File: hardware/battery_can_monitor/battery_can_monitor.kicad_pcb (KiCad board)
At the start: 2 copper layers, 70 x 90 mm, 71 parts, among them J1 sense3, J10 int, J11 GPIO, J12 GPIO, J13 power, J14 CAN_PWR, J15 CANGND, J2 sense1, J3 Conn_01x05_Male, J4 RJ45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

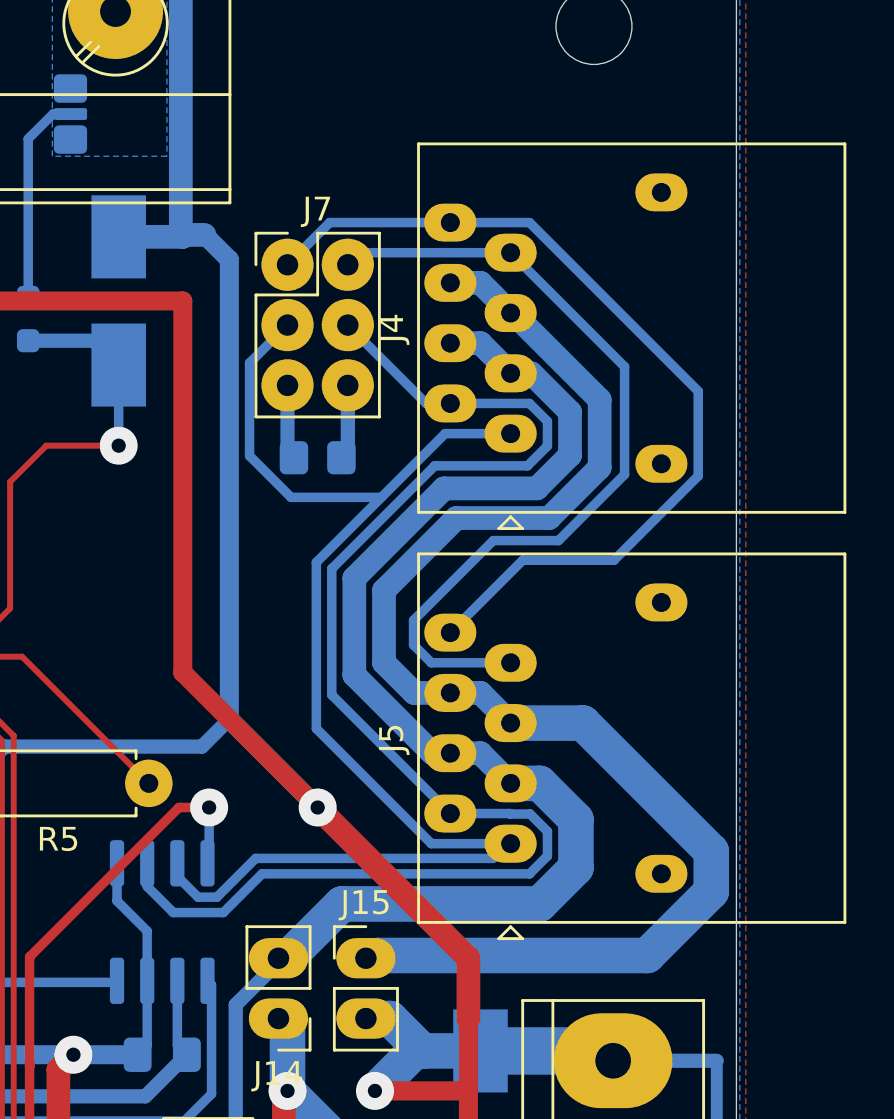
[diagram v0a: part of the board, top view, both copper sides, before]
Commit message: Restore proper hole size for RJ45 connectors.
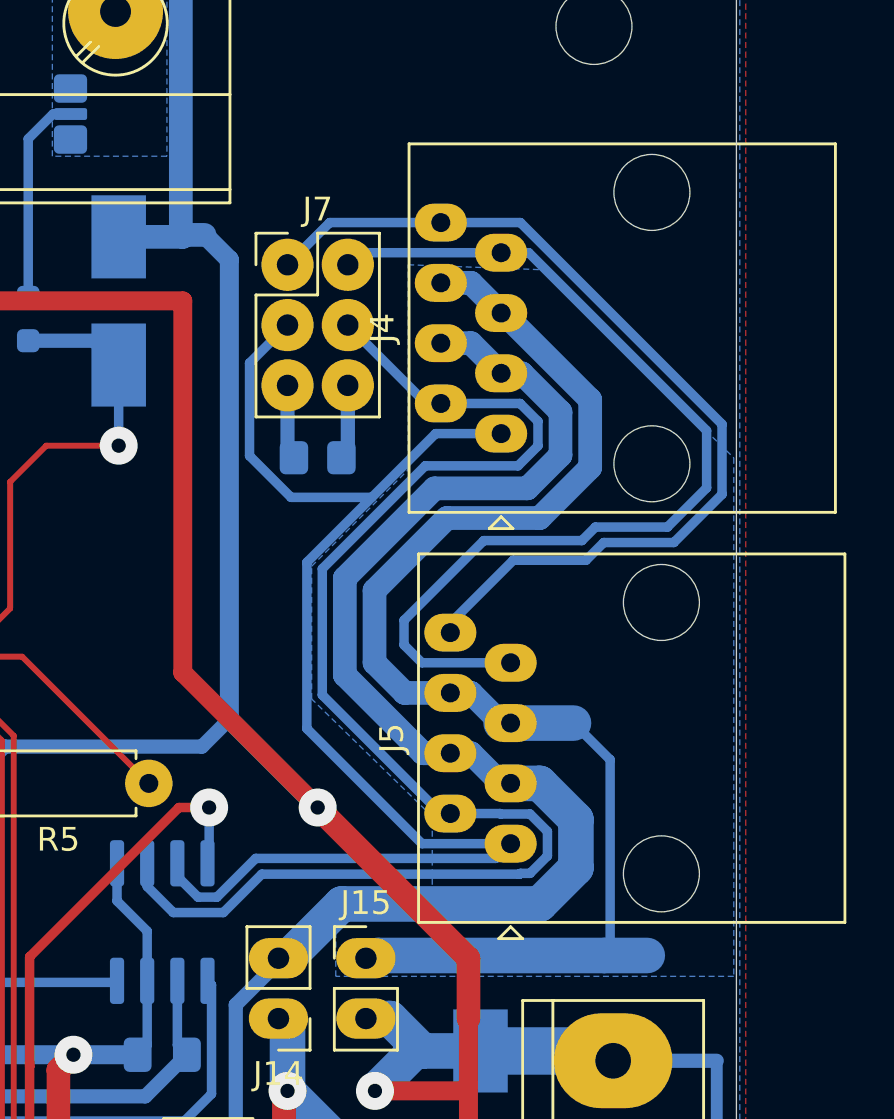
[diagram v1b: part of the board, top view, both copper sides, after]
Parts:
- moved J4 0.40 mm to (110.1, 73.2)
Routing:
- net Net-(J4-Pad7): track 35.3 -> 41.7 mm
- net /CANGND: track 59.6 -> 56.9 mm
- net Net-(J4-Pad8): track 37.7 -> 40.2 mm
- net /CANL: track 59.4 -> 58.8 mm
- added copper zone on B.Cu, net /CANGND
